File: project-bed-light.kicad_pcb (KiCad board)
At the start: 2 copper layers, 24 parts, among them J1 2060-452_998-404, J2 WAGO_2060-453-998-404, J3 Conn_01x03_Pin, Q1 Q_Toshiba_SSM3J328R, U1 TPS62933, U2 Pink Panda v2.1.0

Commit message: pcb: first placement
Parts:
- removed H2: MountingHole_Pad, MountingHole:MountingHole_2.7mm_M2.5_ISO7380_Pad
- added C8: C_Polarized, Capacitor_SMD:CP_Elec_10x10, F.Cu at (60.0, 45.0)
- R2: footprint SMD:0603_1608Metric_DNI_NoPaste -> Resistor_SMD:R_0603_1608Metric
- moved S1 235.5 mm to (17.0, 34.0), turned to 90 degrees
- moved H3 230.6 mm to (15.0, 74.0)
- moved J3 229.6 mm to (20.0, 65.5), turned to 180 degrees
- moved H1 228.2 mm to (15.0, 24.0)
- moved U3 211.6 mm to (39.0, 32.0), turned to -90 degrees
- moved D1 193.5 mm to (46.0, 72.0), turned to 90 degrees
- moved J1 191.4 mm to (57.0, 68.0), turned to 90 degrees
- moved R1 190.8 mm to (45.0, 70.0), turned to 180 degrees
- moved J2 190.7 mm to (60.0, 31.0), turned to 180 degrees
- moved Q1 186.9 mm to (49.0, 72.0)
- moved C3 179.9 mm to (26.5, 63.0), turned to 180 degrees
- moved R2 177.6 mm to (26.5, 65.0), turned to 0 degrees
- moved C4 177.5 mm to (29.5, 63.0), turned to 0 degrees
- moved L1 176.0 mm to (34.5, 61.0), turned to 0 degrees
- moved H4 175.1 mm to (67.0, 74.0)
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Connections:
- net /Reverse Polarity Protection/OUT renamed /regulator_in
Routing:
- net +5V: track 0.00 -> 25.6 mm, vias 0 -> 2
- net Net-(U1-SS): track 0.00 -> 3.72 mm

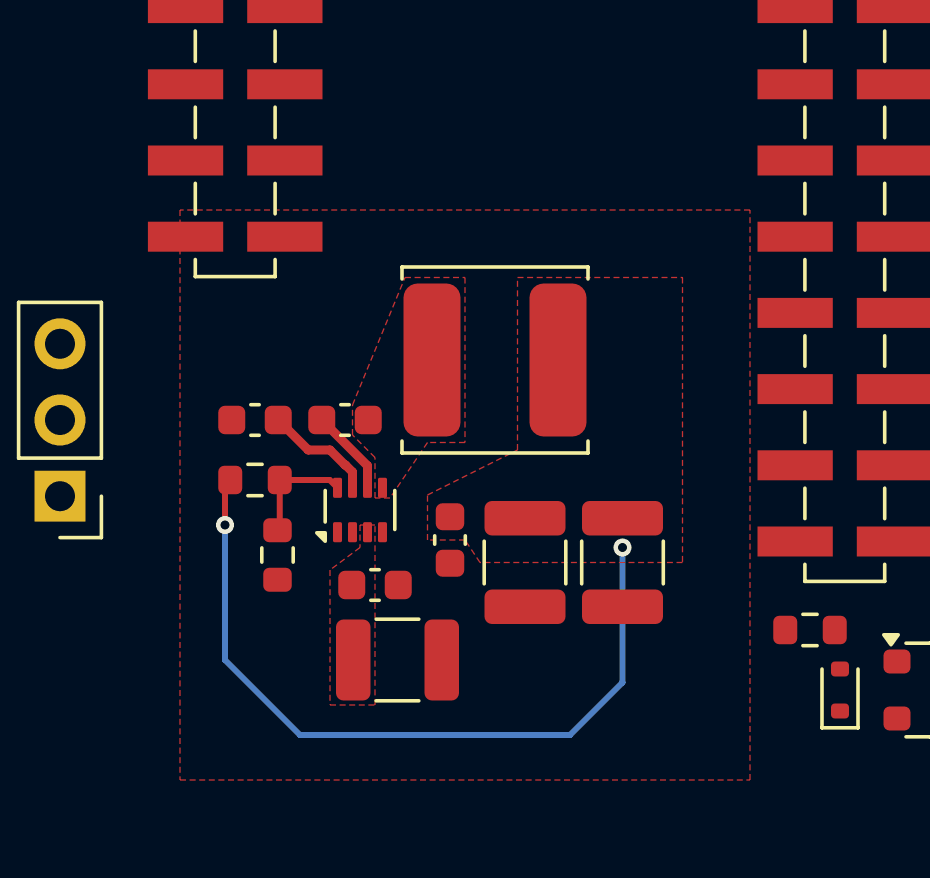
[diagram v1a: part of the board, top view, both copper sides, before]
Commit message: pcb: rotate regulator section
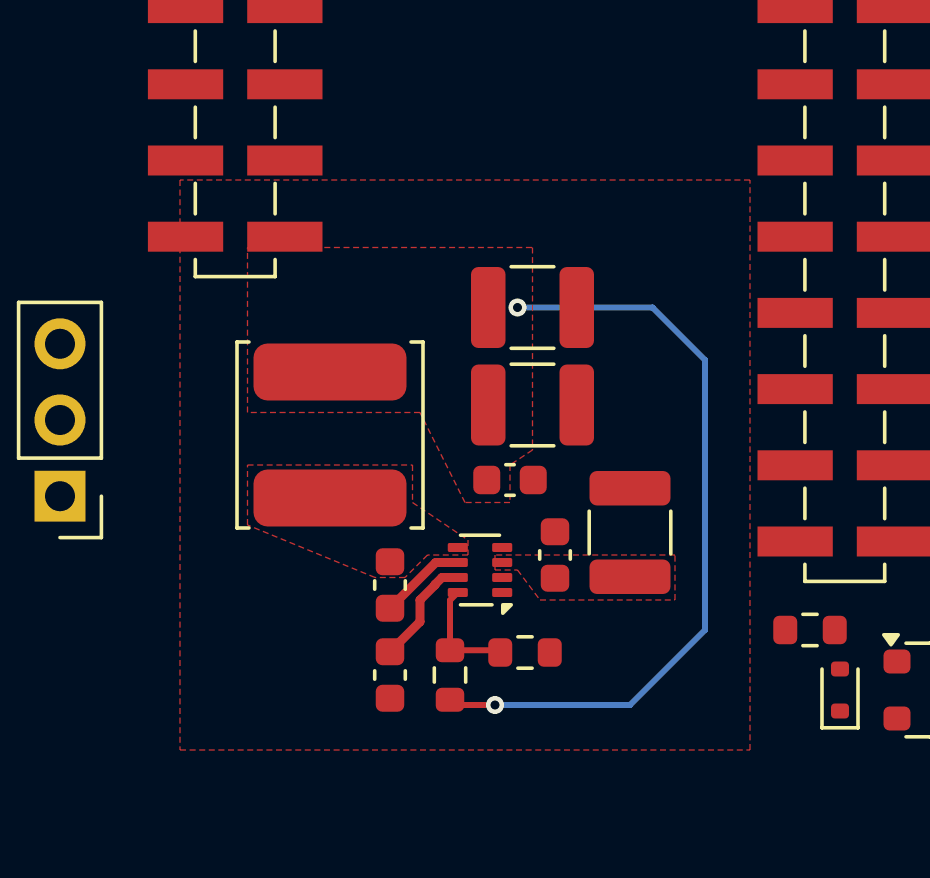
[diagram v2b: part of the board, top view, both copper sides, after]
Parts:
- moved C3 9.62 mm to (31.0, 71.5), turned to -90 degrees
- moved R2 9.19 mm to (33.0, 71.5), turned to 90 degrees
- moved C7 9.01 mm to (35.8, 59.2), turned to 0 degrees
- moved R3 8.87 mm to (35.5, 70.8), turned to 0 degrees
- moved C1 8.84 mm to (39.0, 66.8), turned to 90 degrees
- moved C2 6.08 mm to (36.5, 67.5), turned to 90 degrees
- moved L1 6.04 mm to (29.0, 63.5), turned to 90 degrees
- moved C4 5.70 mm to (31.0, 68.5), turned to 90 degrees
- moved C6 5.26 mm to (35.8, 62.5), turned to 0 degrees
- moved U1 4.47 mm to (34.0, 68.0), turned to 180 degrees
- moved C5 2.83 mm to (35.0, 65.0), turned to 0 degrees

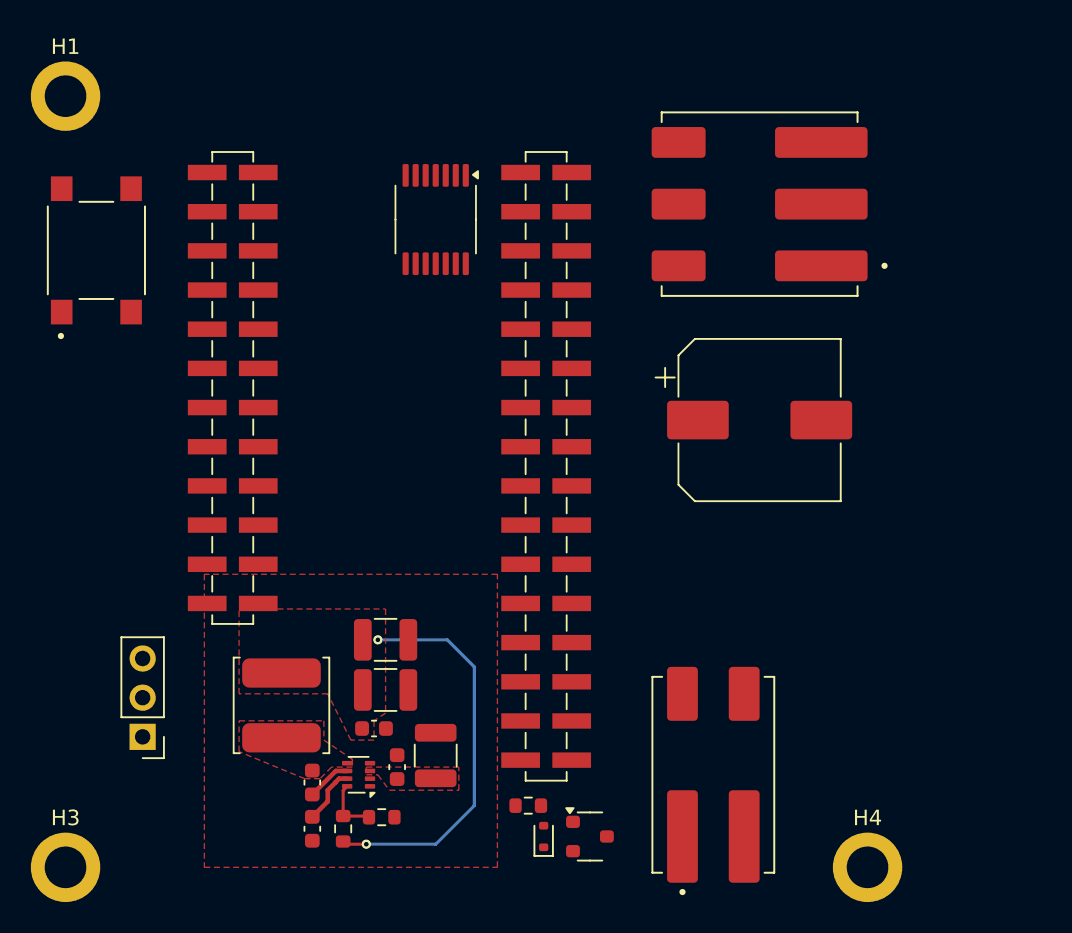
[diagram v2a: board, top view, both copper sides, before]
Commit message: pcb: route 24V
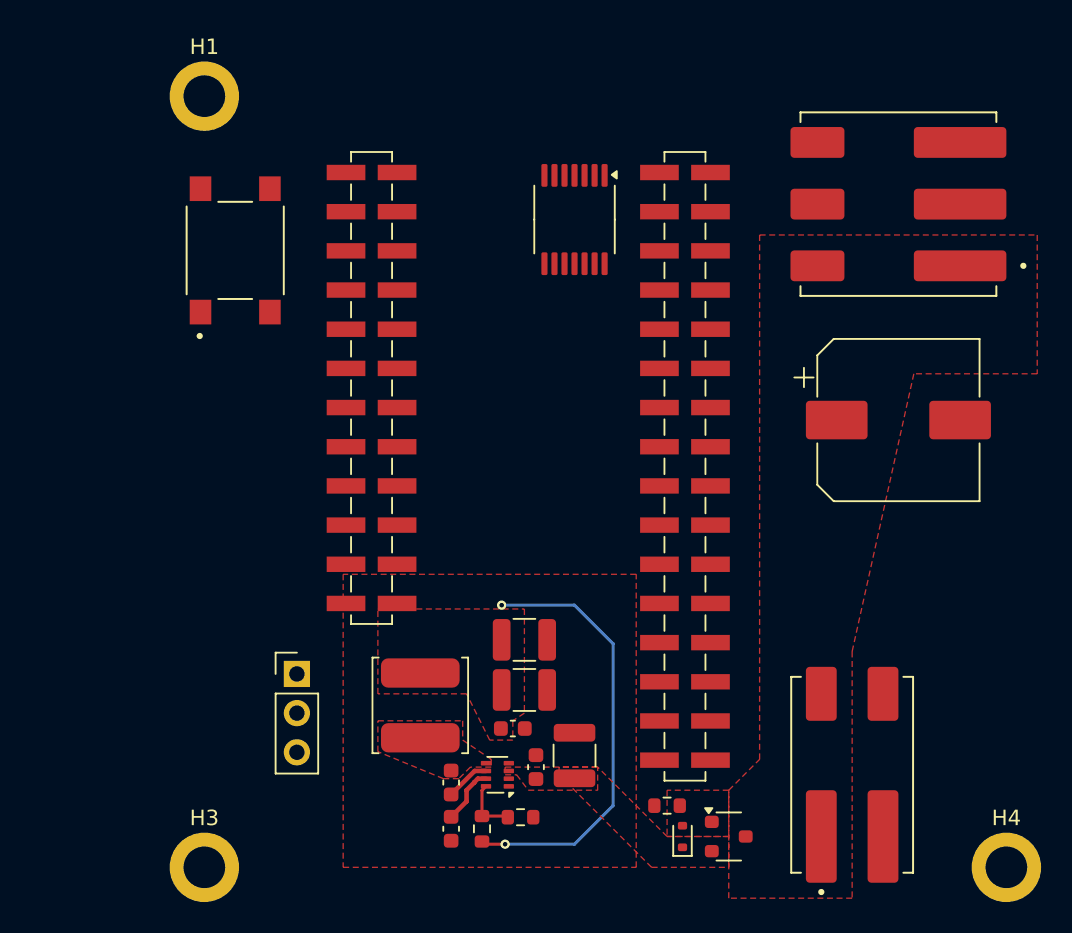
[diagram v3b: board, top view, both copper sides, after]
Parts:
- moved J3 10.8 mm to (30.0, 61.5), turned to 0 degrees
- moved C1 9.00 mm to (48.0, 66.8)
- moved C2 9.00 mm to (45.5, 67.5)
- moved C3 9.00 mm to (40.0, 71.5)
- moved C4 9.00 mm to (40.0, 68.5)
- moved C5 9.00 mm to (44.0, 65.0)
- moved C6 9.00 mm to (44.8, 62.5)
- moved C7 9.00 mm to (44.8, 59.2)
- moved C8 9.00 mm to (69.0, 45.0)
- moved D1 9.00 mm to (55.0, 72.0)
- moved H1 9.00 mm to (24.0, 24.0)
- moved H3 9.00 mm to (24.0, 74.0)
- moved H4 9.00 mm to (76.0, 74.0)
- moved J1 9.00 mm to (66.0, 68.0)
- moved J2 9.00 mm to (69.0, 31.0)
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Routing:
- net +5V: track 25.6 -> 28.4 mm
- added copper zone on F.Cu, net +24V
- added copper zone on F.Cu, net Net-(D1-A)

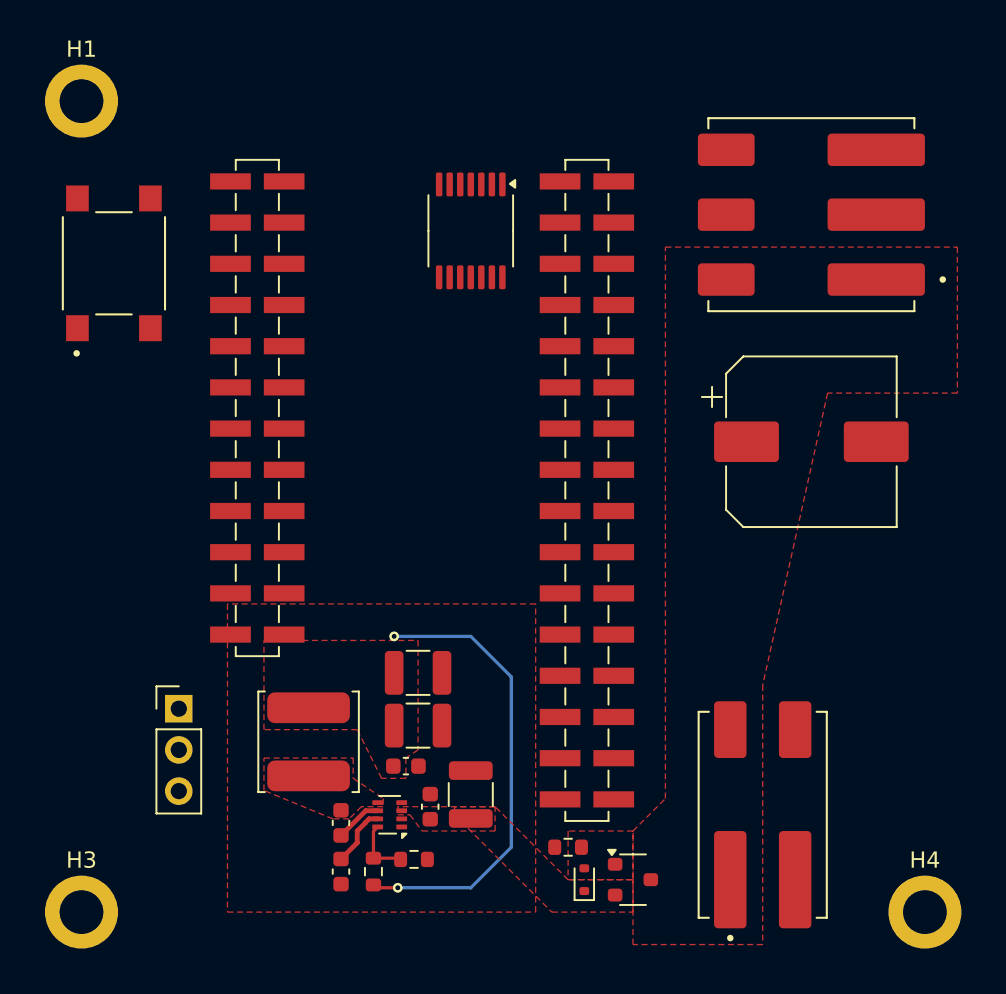
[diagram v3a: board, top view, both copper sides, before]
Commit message: pcb: route all power
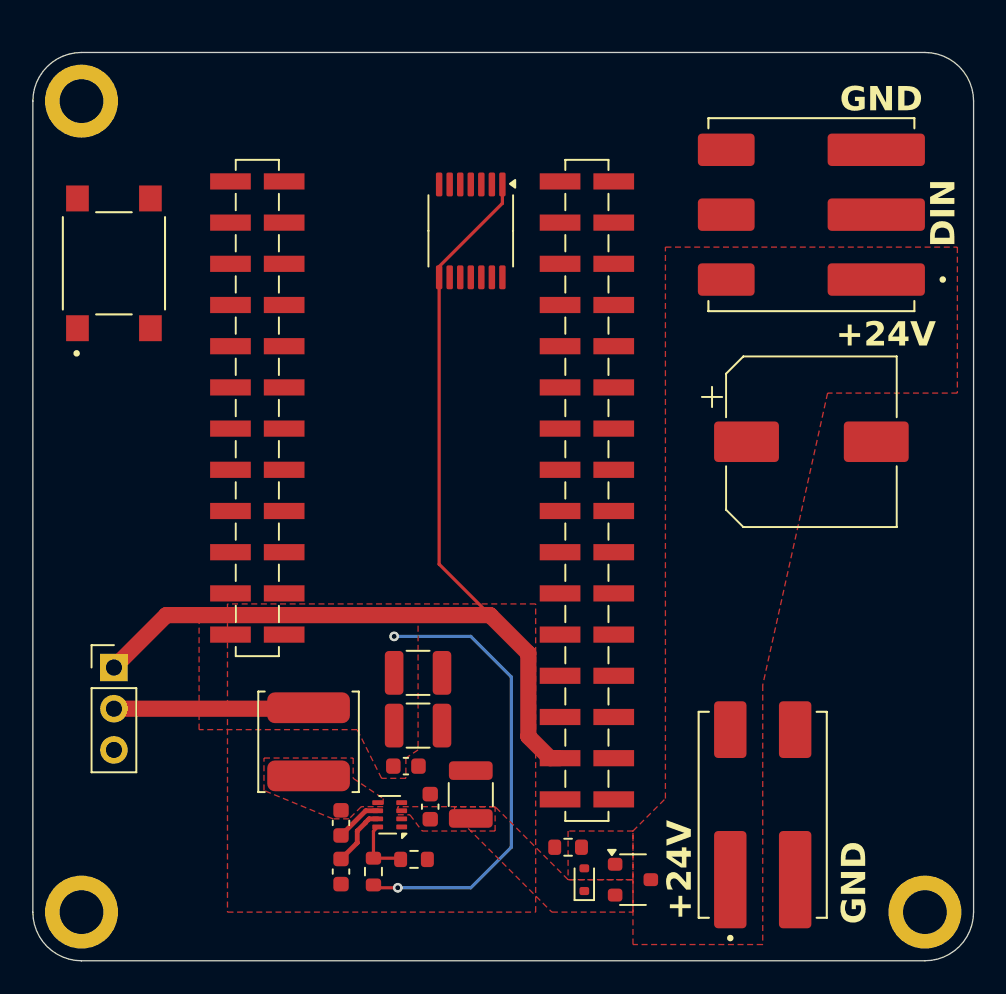
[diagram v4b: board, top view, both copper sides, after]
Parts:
- moved J3 4.74 mm to (26.0, 58.9)
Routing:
- net +3.3V: track 0.00 -> 65.0 mm
- net +5V: track 28.4 -> 40.4 mm
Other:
- board outline added: 58 x 56 mm
- board text added: "+24V"
- board text added: "DIN"
- board text added: "GND"
